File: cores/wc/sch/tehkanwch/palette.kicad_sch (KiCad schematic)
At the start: 21 parts

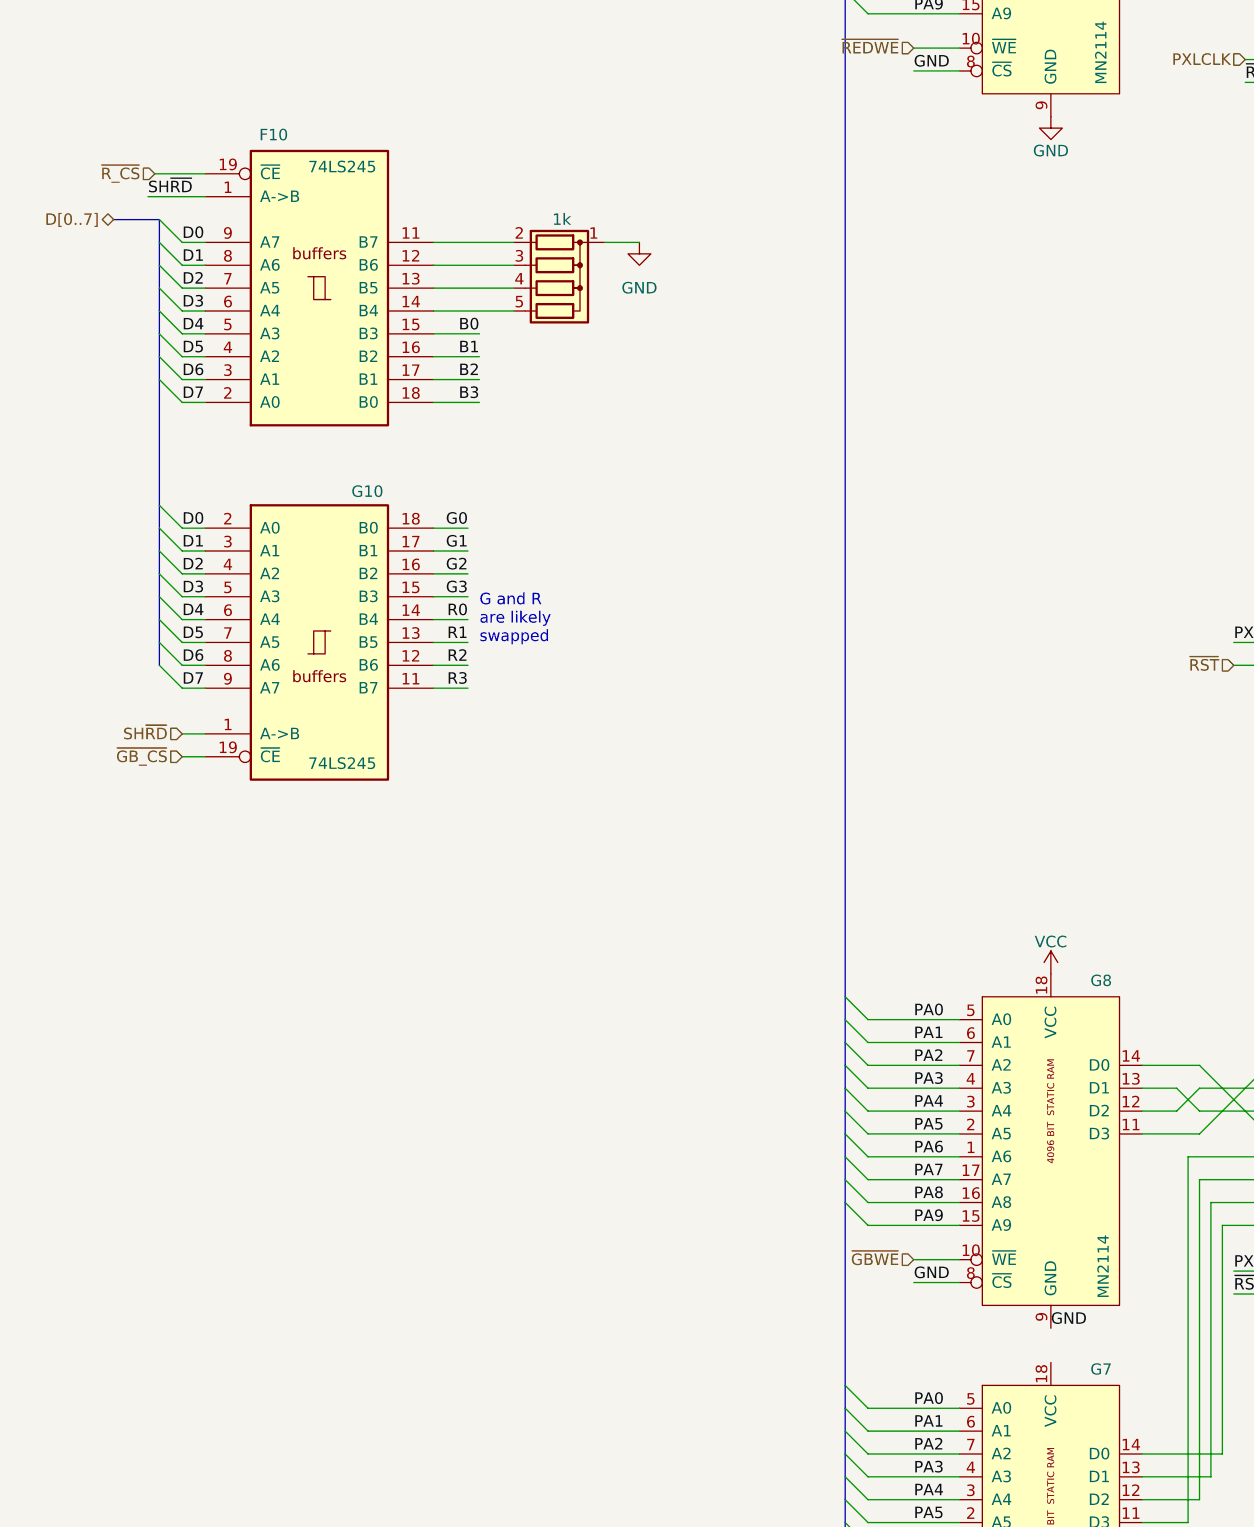
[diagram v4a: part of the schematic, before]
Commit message: wc: tehkanwch schematics completed. ERC clean
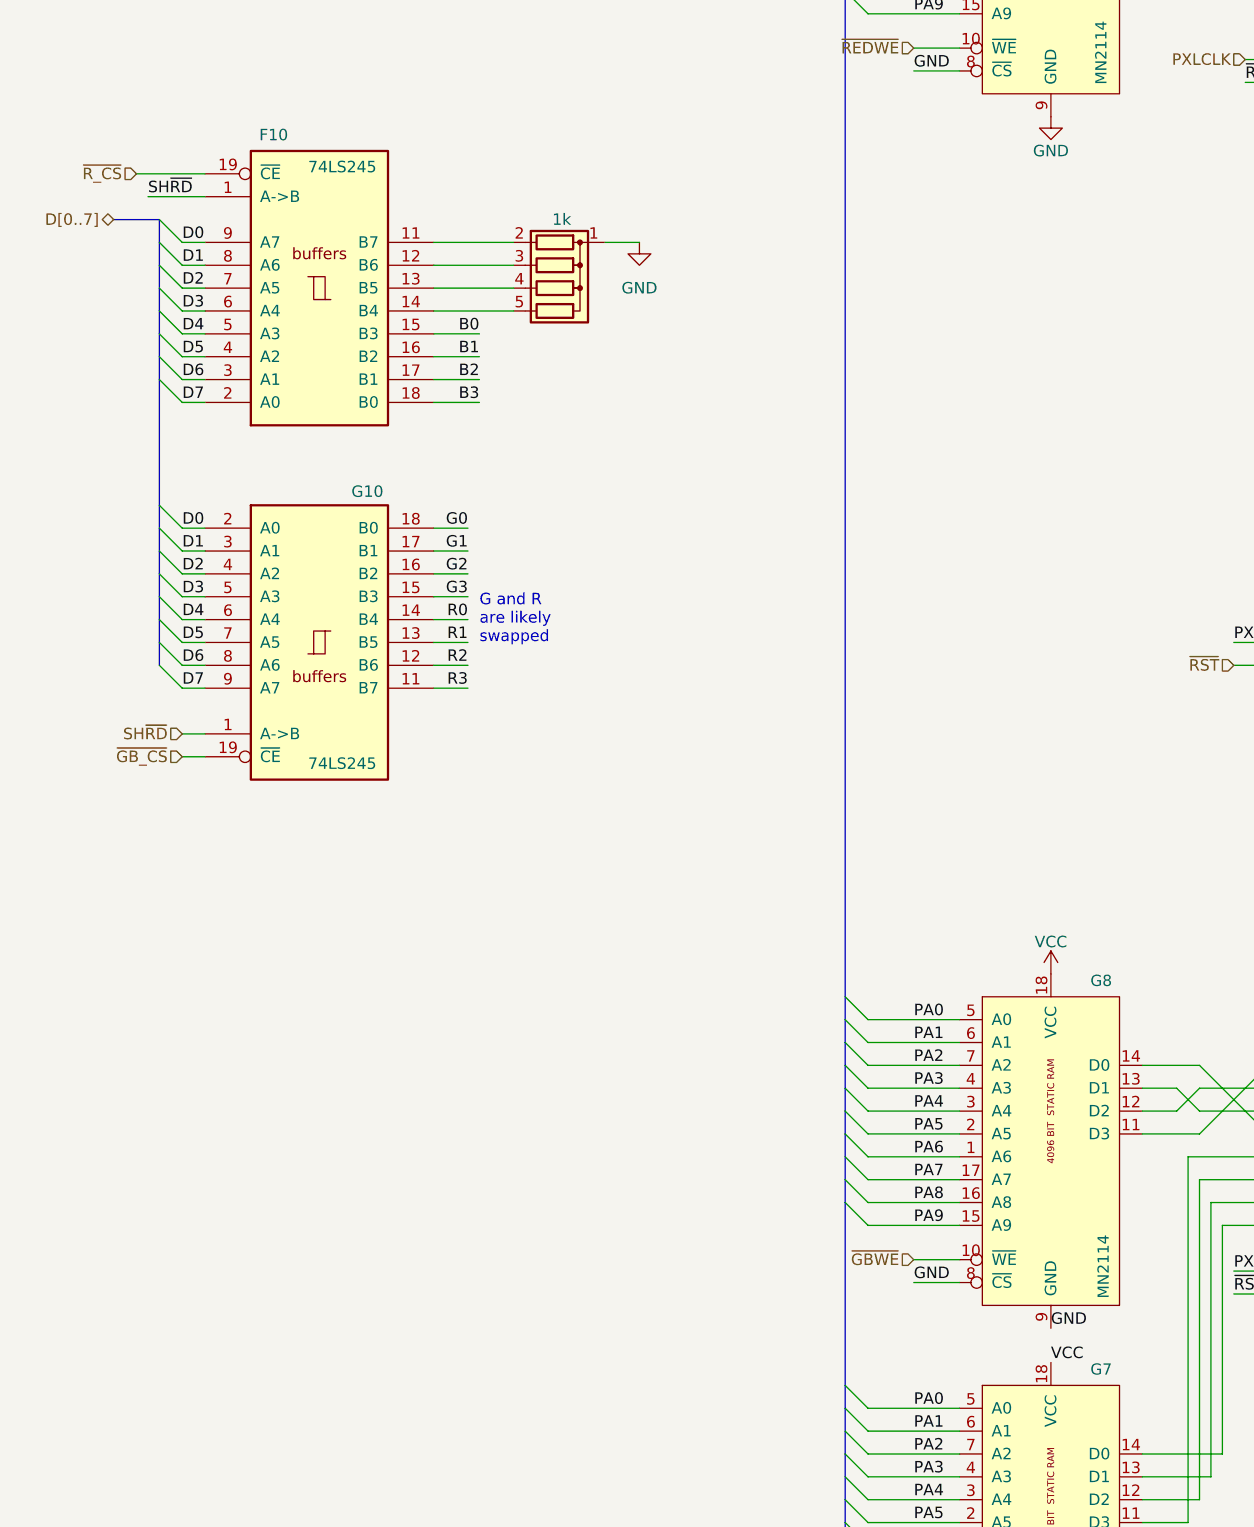
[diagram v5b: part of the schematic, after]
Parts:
- renumbered RN3 to RP0
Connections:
- net VCC: now also G7.18 (VCC)
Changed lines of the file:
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@@
 	(title_block
 		(title "Color Palette")
-		(date "2024-10-12")
+		(date "2024-11-15")
 		(company "JOTEGO")
-		(comment 1 "Jose Tejada")
+		(comment 1 "https://www.patreon.com/jotego")
+		(comment 2 "Jose Tejada")
 	)
 	(junction
@@
 	(wire
 		(pts
-			(xy 104.902 101.6) (xy 110.49 101.6)
+			(xy 102.87 101.6) (xy 110.49 101.6)
 		)
 		(stroke
@@
 		)
 	)
+	(label "VCC"
+		(at 204.47 233.68 0)
+		(fields_autoplaced yes)
+		(effects
+			(font
+				(size 1.27 1.27)
+			)
+			(justify left bottom)
+		)
+	)
 	(label "GND"
 		(at 269.24 166.37 0)
@@
 	(hierarchical_label "~{R_CS}"
 		(shape input)
-		(at 104.902 101.6 180)
+		(at 102.87 101.6 180)
 		(fields_autoplaced yes)
 		(effects
@@
 		(on_board yes)
 		(dnp no)
-		(property "Reference" "RN3"
+		(property "Reference" "RP0"
 			(at 149.606 123.19 90)
 			(effects
@@
 			(project "tehkanwch"
 				(path "/f324726e-ed6b-4b88-9562-4b07e126a276/4d18f4f6-4d7d-4823-941f-121a8e5c871f/e275c20e-58da-4787-bf27-1e3b67330979"
-					(reference "RN3")
+					(reference "RP0")
 					(unit 1)
 				)
